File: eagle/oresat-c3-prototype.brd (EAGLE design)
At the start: 99.8 x 94.7 mm, 108 parts, among them J1 J-SAMTEC-TFM-110-X1-XXX-D-RA, J10 2X8X1.27, J11 2X8X1.27, J12 2X8X1.27, J2 U.FL, J3 U.FL, J4 U.FL, J6 J-SAMTEC-TFM-120-X1-XXX-D-RA, J7 FTSH-105-XX-X-DV-K, J8 SD_CARD_SOCKET, J9 2X8X1.27, Q1 MOSFET-PCH-SOT23-6, Q2 MOSFET-PCH-SOT23-6, U1 MAX892LEUA+T, U2 TCAN330, U3 TCAN330, U4 TPS259621 - eFuse, U5 TPS62111RSA, U6 MAX6373KA+21-0078H-L, U7 STM32F446RE, X1 16MHZ-2.5x2mm

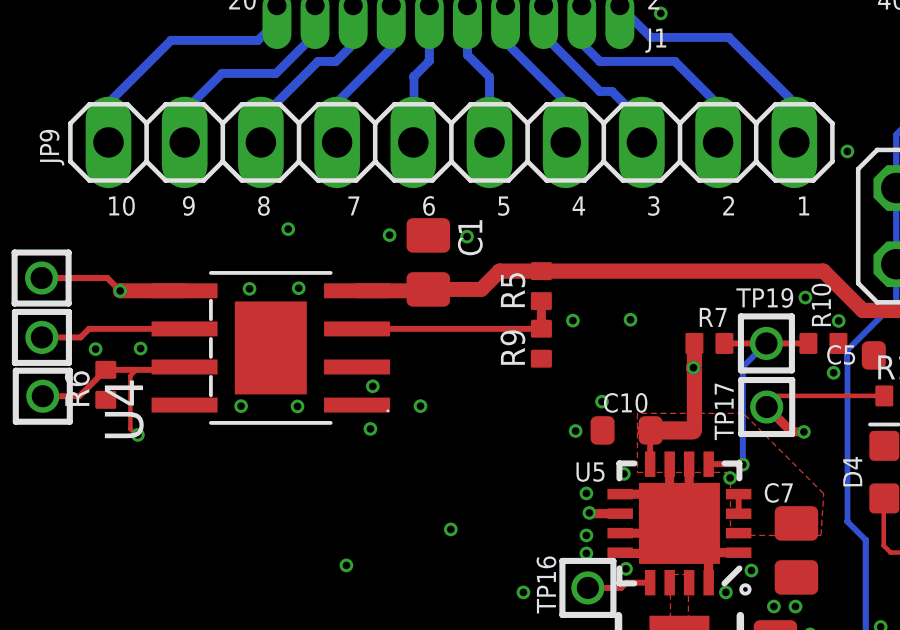
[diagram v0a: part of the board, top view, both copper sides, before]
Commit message: Fixed some additional stubs and air wires
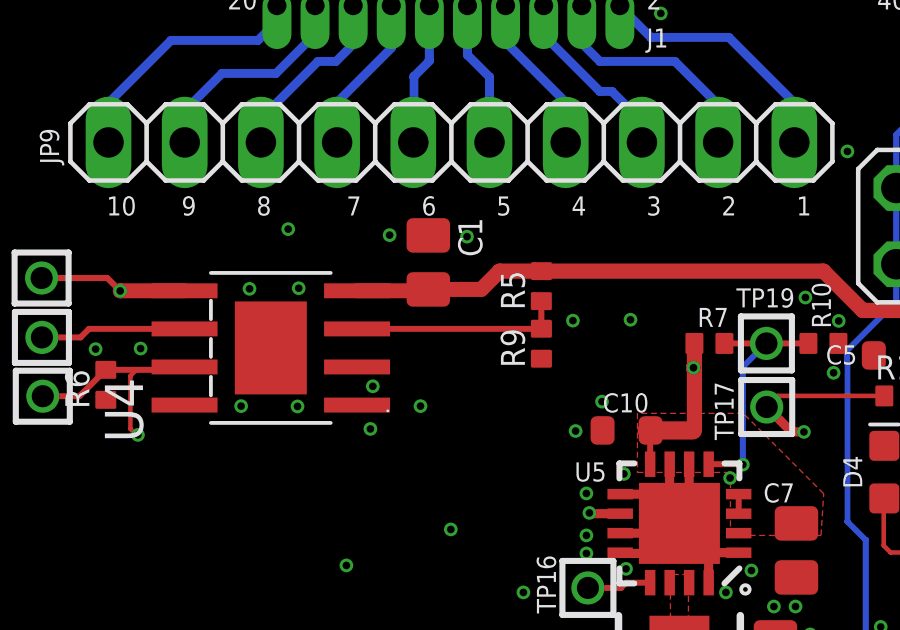
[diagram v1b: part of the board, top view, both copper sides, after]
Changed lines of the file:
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@@
 <?xml version="1.0" encoding="utf-8"?>
 <!DOCTYPE eagle SYSTEM "eagle.dtd">
-<eagle version="9.5.1">
+<eagle version="9.5.2">
 <drawing>
 <settings>
@@
 <contactref element="R5" pad="1"/>
 <contactref element="U4" pad="3"/>
-<wire x1="18.855" y1="76.585" x2="24.993253125" y2="76.585" width="0.2" layer="1"/>
-<wire x1="24.998253125" y1="77.51" x2="24.998253125" y2="76.59" width="0.3048" layer="1"/>
-<wire x1="24.998253125" y1="76.59" x2="24.993253125" y2="76.585" width="0.3048" layer="1"/>
-<wire x1="24.998253125" y1="77.51" x2="25" y2="76.59" width="0" layer="19" extent="1-1"/>
+<wire x1="18.855" y1="76.585" x2="24.995" y2="76.585" width="0.2" layer="1"/>
+<wire x1="24.995" y1="76.585" x2="25" y2="76.59" width="0.2" layer="1"/>
+<wire x1="25" y1="76.59" x2="24.998253125" y2="76.591746875" width="0.2" layer="1"/>
+<wire x1="24.998253125" y1="76.591746875" x2="24.998253125" y2="77.51" width="0.2" layer="1"/>
 </signal>
 <signal name="CB_IOUT">

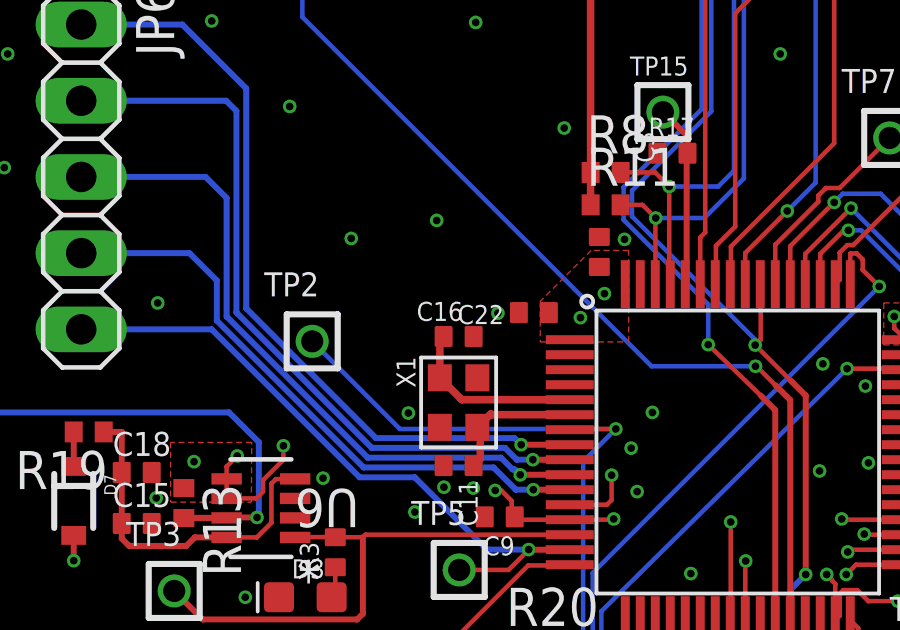
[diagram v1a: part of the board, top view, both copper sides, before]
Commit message: Added TP for one last MCU pin
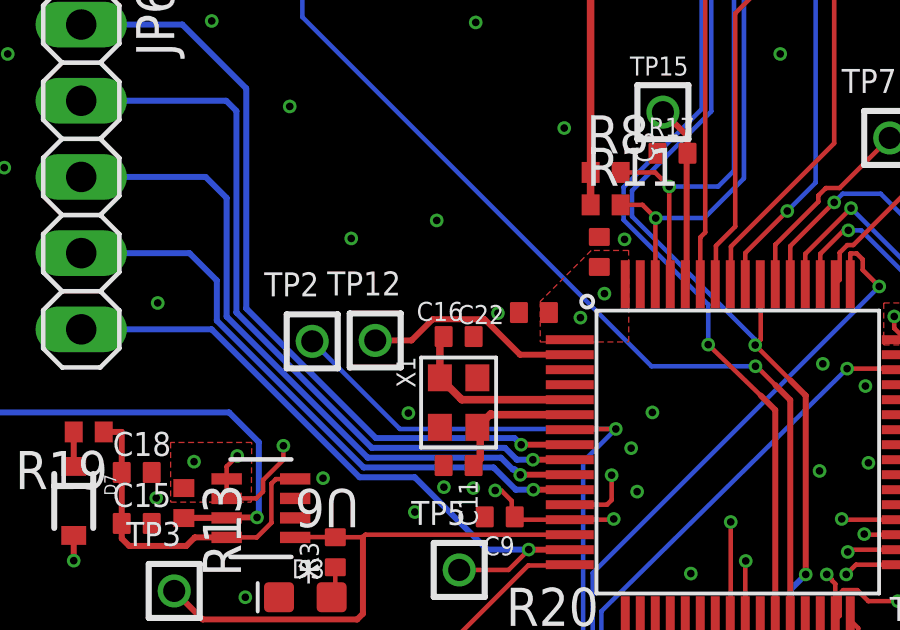
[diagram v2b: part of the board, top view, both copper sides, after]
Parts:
- added TP12: TEST-POINT, Tova:2MM-TEST-POINT
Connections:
- net PC13: now also TP12.1
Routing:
- net PC13: track 0.00 -> 7.27 mm
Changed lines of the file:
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@@
 <attribute name="VENDOR" value="Maxim Integrated Products" x="41.595" y="74.72" size="1.778" layer="27" display="off"/>
+</element>
+<element name="TP12" library="Tova" package="2MM-TEST-POINT" value="TEST-POINT" x="41.9" y="49.6" smashed="yes">
+<attribute name="NAME" x="40.3" y="51.1" size="0.8" layer="25" font="vector" ratio="20"/>
 </element>
 </elements>
@@
 <signal name="PC13">
 <contactref element="U7" pad="2"/>
+<contactref element="TP12" pad="1"/>
+<wire x1="45.54415" y1="50.307" x2="43.81585" y2="50.307" width="0.2" layer="1"/>
+<wire x1="48.385" y1="49.125" x2="46.72615" y2="49.125" width="0.2" layer="1"/>
+<wire x1="43.10885" y1="49.6" x2="41.9" y2="49.6" width="0.2" layer="1"/>
+<wire x1="46.72615" y1="49.125" x2="45.54415" y2="50.307" width="0.2" layer="1"/>
+<wire x1="43.81585" y1="50.307" x2="43.10885" y2="49.6" width="0.2" layer="1"/>
 </signal>
 <signal name="OSC32_IN">

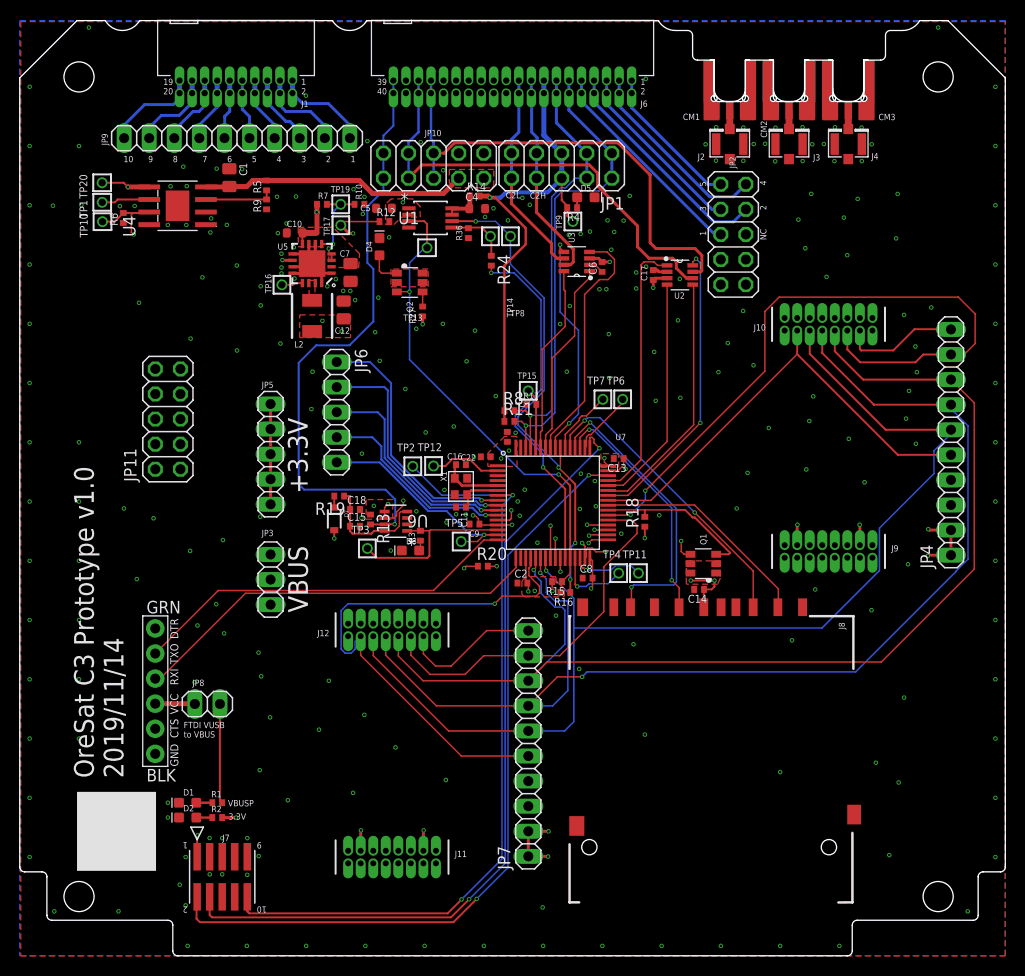
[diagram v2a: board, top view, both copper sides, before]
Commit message: Polishing by mysterious outside forces. Schematic cleanup, including removing some unecessary components, moved radios and MMC carrier to actually fit on the card, moved power around to be more optimally connected, cleaned up lots of routing.
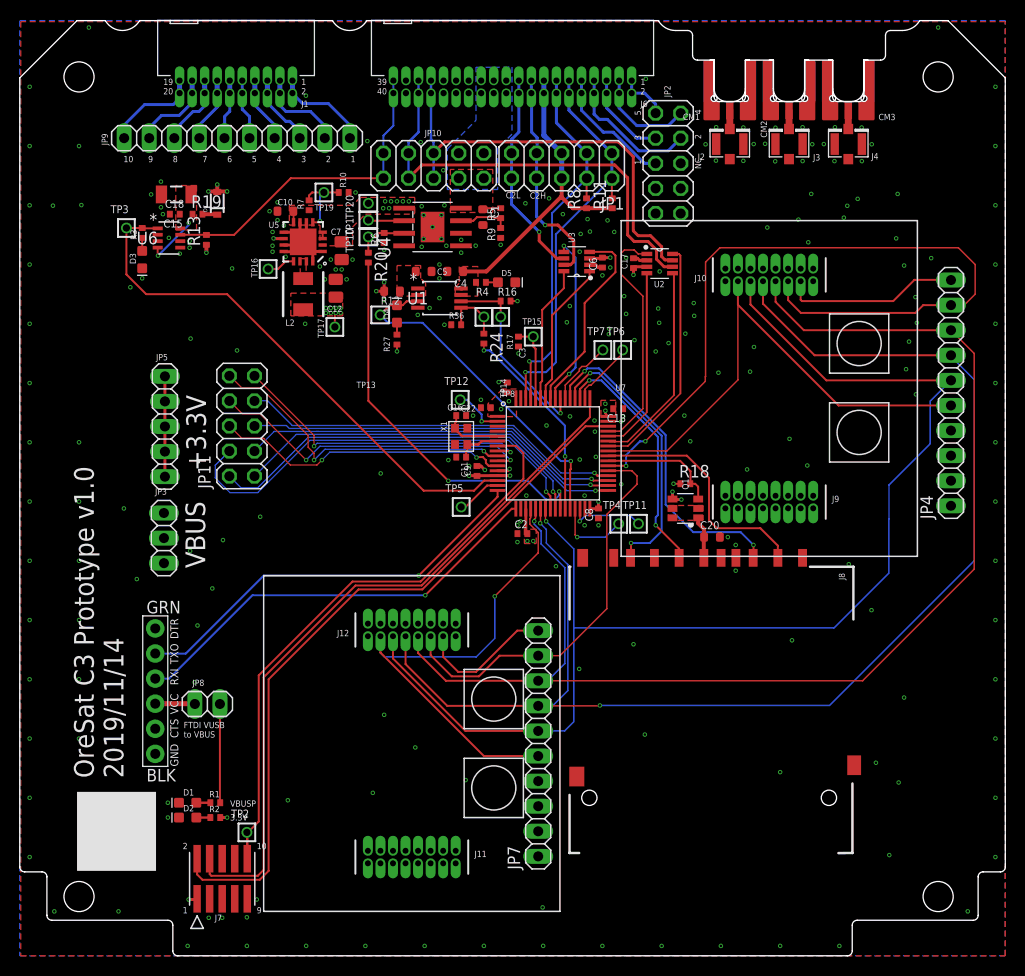
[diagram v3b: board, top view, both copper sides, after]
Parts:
- removed C14: 1u, rcl_custom:.0402-B-NOSILK
- removed JP6: (no value), pinhead:1X05
- removed Q2: MOSFET-PCH-SOT23-6, Q-MOSFET-PCH-SOT23-6:SOT23-6
- removed R14: 0, rcl_custom:.0402-B-NOSILK
- removed R15: 10k, rcl_custom:.0402-B-NOSILK
- removed TP9: TEST-POINT, Tova:2MM-TEST-POINT
- added C20: 1u, oresat-rcl:.0603-B-NOSILK
- C1: device oresat-rcl:.0805-B-NOSILK -> oresat-rcl:.0603-B-NOSILK
- C13, C15, C16, C17, C2, C22, C3, C6, C8, C9, R1, R10, R16, R17, R2, R27, R3, R36, R4, R5, R6, R7, R9: device rcl_custom:.0402-B-NOSILK -> oresat-rcl:.0402-B-NOSILK
- C18: value 100u -> 47u; device rcl_custom:.0402-B-NOSILK -> oresat-rcl:1206-B
- C4: value 0.1u -> 1u
- R11, R13, R18, R19, R20, R24, R8: device rcl:R0402 -> oresat-rcl:.0402-B-NOSILK
- R12: device rcl_custom:.0402-B-NOSILK -> oresat-rcl:.0603-B-NOSILK
- moved R3 41.6 mm to (12.4, 73.2)
- moved TP2 40.7 mm to (23.0, 12.5)
- moved TP3 40.6 mm to (10.8, 73.7)
- moved D3 40.1 mm to (12.4, 70.5), turned to 270 degrees
- moved U6 36.8 mm to (15.1, 72.7), turned to 0 degrees
- moved C18 36.7 mm to (15.8, 77.1), turned to 180 degrees
- moved C15 36.5 mm to (15.7, 75.1), turned to 180 degrees
- moved D7 34.1 mm to (20.0, 76.2), turned to 90 degrees
- moved R20 33.3 mm to (35.3, 70.7), turned to 270 degrees
- moved R13 32.8 mm to (18.9, 72.5), turned to 90 degrees
- moved R19 32.0 mm to (18.0, 75.1), turned to 0 degrees
- moved R16 30.1 mm to (49.2, 66.3), turned to 0 degrees
- moved TP20 27.0 mm to (35.3, 76.2)
- moved TP1 27.0 mm to (35.3, 74.5)
- moved TP10 27.0 mm to (35.3, 72.8)
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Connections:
- net N$4 renamed WDT-PWR
- removed net OPD_ON/LED: D4.A, Q2.1, Q2.2, Q2.5, Q2.6
- removed net OPD_ON/LED_SWITCH: Q2.4, R27.1
- new net N$5: D4.A, R27.1
- new net OPD-3.3V: C5.1, R12.1, U1.1, U1.2
- net !OPD_ENABLE: now also D4.C; no longer Q2.3, R15.1
- net 3.3V: no longer C5.1, R12.1, R15.2, U1.1, U1.2
- net GND: now also C1.2, C20.2; no longer C1.1, C14.2, D4.C
- net MMC_VDD: now also C20.1; no longer C14.1
- net OPD_PWR: no longer R14.1, R14.2, TP9.1
- net PA1: no longer JP6.5
- net PC0: no longer JP6.1
- net PC1: no longer JP6.2
- net PC2: no longer JP6.3
- net PC3: no longer JP6.4
- net VBUS: now also C1.1; no longer C1.2
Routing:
- net CB_IOUT: track 57.2 -> 5.41 mm, vias 2 -> 0
- net WDT: track 18.5 -> 55.0 mm
- net CB_IOUT_IN: track 9.46 -> 39.9 mm
- net OPD_!FAULT: track 49.8 -> 19.6 mm, vias 4 -> 1
- net !SD: track 62.7 -> 33.3 mm, vias 1 -> 0
- net 3.3V: track 65.2 -> 37.4 mm, vias 32 -> 40
- net VBUS: track 27.0 -> 1.84 mm
- net OPD_PWR: track 53.8 -> 31.3 mm, vias 1 -> 0
- net NRST: track 79.8 -> 62.3 mm, vias 2 -> 0
- net PA1: track 21.9 -> 4.59 mm, vias 1 -> 0
- net OPD_ISET_IN: track 36.2 -> 20.5 mm
- net SPI1_MOSI: track 114.0 -> 128.9 mm
- net !OPD_ENABLE: track 49.5 -> 34.7 mm, vias 2 -> 1
- net SPI1_MISO: track 123.0 -> 136.7 mm
- net SPI1_SCK: track 117.0 -> 130.5 mm
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- added copper zone on layer 15, net GND
- added copper zone on layer 1, net OPD-3.3V
- added copper zone on layer 1, net OPD_PWR
- added copper zone on layer 16, net VBUS
- added copper zone on layer 15, net VBUSP
- added copper zone on layer 1, net WDT-PWR
- removed copper zone on layer 1, net OPD_ON/LED
- removed copper zone on layer 15, net VBUS

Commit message: Fix VCAP, fix JTAG header, remove weird 0.1in headers which make SPI bus go everywhere, fix component tyes, add test points, polish.
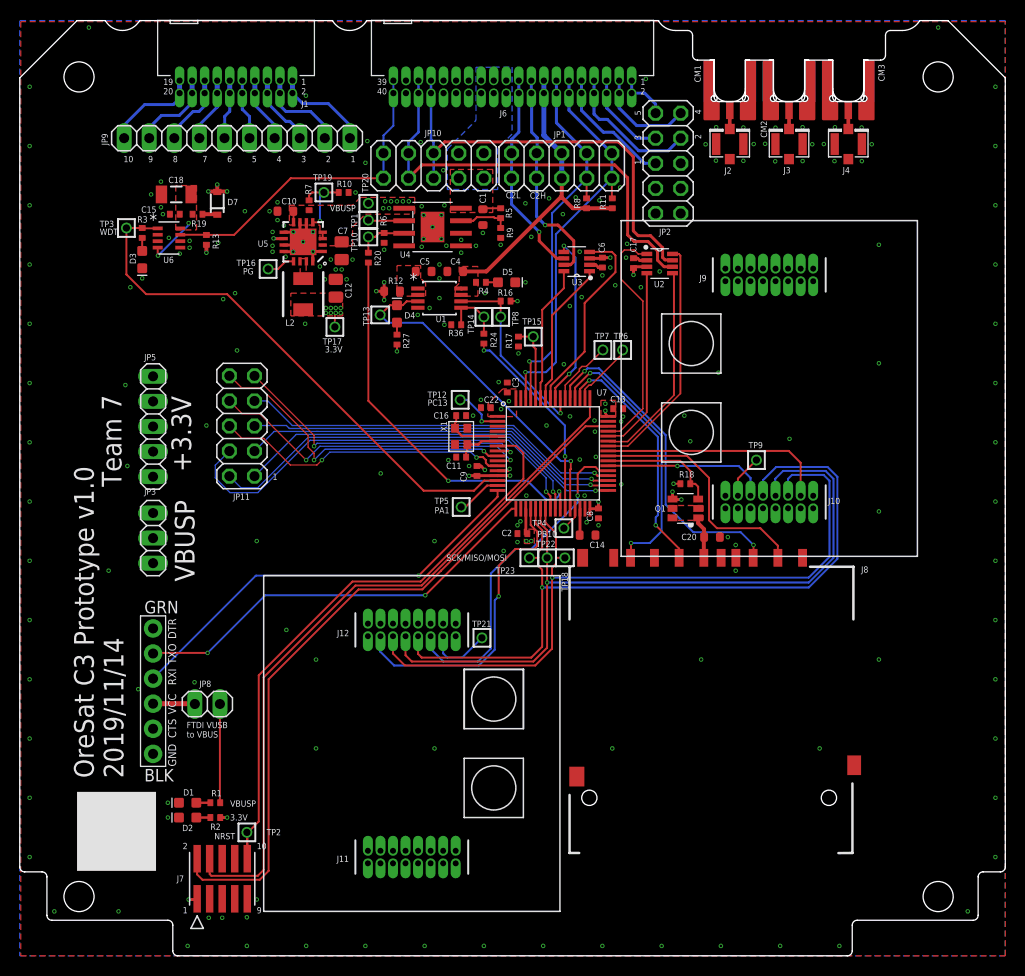
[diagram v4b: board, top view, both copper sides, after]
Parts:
- removed JP4, JP7: (no value), pinhead:1X10
- removed TP11: TEST-POINT, Tova:2MM-TEST-POINT
- added C14: 2.2u, oresat-rcl:.0603-B-NOSILK
- added TP18, TP21, TP22, TP23, TP9: TEST-POINT, Tova:2MM-TEST-POINT
- D3: value AMBER -> RED
- moved J10 23.0 mm to (75.9, 46.0), turned to 0 degrees
- moved J9 23.0 mm to (75.9, 69.0), turned to 180 degrees
- moved TP4 5.57 mm to (55.1, 43.3)
- moved JP5 1.20 mm to (13.5, 53.6)
- moved JP3 1.10 mm to (13.5, 42.3)
- moved J5 0.22 mm to (13.5, 26.8)
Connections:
- net 3.3V: no longer JP4.1, JP4.2, JP7.1, JP7.2
- net GND: now also C14.2; no longer JP4.3, JP4.4, JP7.3, JP7.4
- net RADIO1_CS: no longer JP7.9
- net RADIO1_IRQ: no longer JP7.5
- net RADIO1_SYSCLK: now also TP21.1; no longer JP7.10
- net RADIO2_CS: no longer JP4.9
- net RADIO2_IRQ: no longer JP4.5
- net RADIO2_SYSCLK: now also TP9.1; no longer JP4.10
- net SPI1_MISO: now also TP22.1; no longer JP4.7, JP7.7
- net SPI1_MOSI: now also TP18.1; no longer JP4.6, JP7.6
- net SPI1_SCK: now also TP23.1; no longer JP4.8, JP7.8
- net USART2_RX: now also J5.P$2; no longer J5.P$3
- net USART2_TX: now also J5.P$3; no longer J5.P$2
- net VCAP: now also C14.1; no longer TP11.1
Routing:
- net RADIO2_CS: track 80.1 -> 16.7 mm, vias 2 -> 1
- net SPI1_MISO: track 136.7 -> 77.8 mm, vias 2 -> 1
- net SPI1_MOSI: track 128.9 -> 77.8 mm
- net SPI1_SCK: track 130.5 -> 79.9 mm
- net RADIO2_IRQ: track 51.9 -> 23.3 mm
- net RADIO1_IRQ: track 51.5 -> 31.9 mm
- net RADIO2_SYSCLK: track 18.1 -> 4.39 mm
- net 3.3V: track 37.4 -> 27.3 mm, vias 40 -> 34
- net RADIO1_SYSCLK: track 14.1 -> 6.67 mm
- net RADIO1_CS: track 41.3 -> 34.3 mm, vias 0 -> 1
- net PB10: track 7.72 -> 2.45 mm, vias 1 -> 0
- net VCAP: track 7.84 -> 2.69 mm, vias 1 -> 0
- net USART2_TX: track 41.9 -> 43.2 mm
- net USART2_RX: track 43.6 -> 42.8 mm, vias 1 -> 2
- net GND: vias 232 -> 205
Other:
- board text added: "NRST"
- board text added: "PA1"
- board text added: "PB10"
- board text added: "PC13"
- board text added: "PG"
- board text added: "SCK/MISO/MOSI"
- board text added: "Team 7"
- board text added: "WDT"
- board text removed: "NC"
- board text removed: "VBUS"
